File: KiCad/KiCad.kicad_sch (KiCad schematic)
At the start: 20 parts, among them J1 DC-IN, J2 USB4105-GF-A, U1 ESP32-WROOM-32E, U2 MP1584EN, U3 CH340C

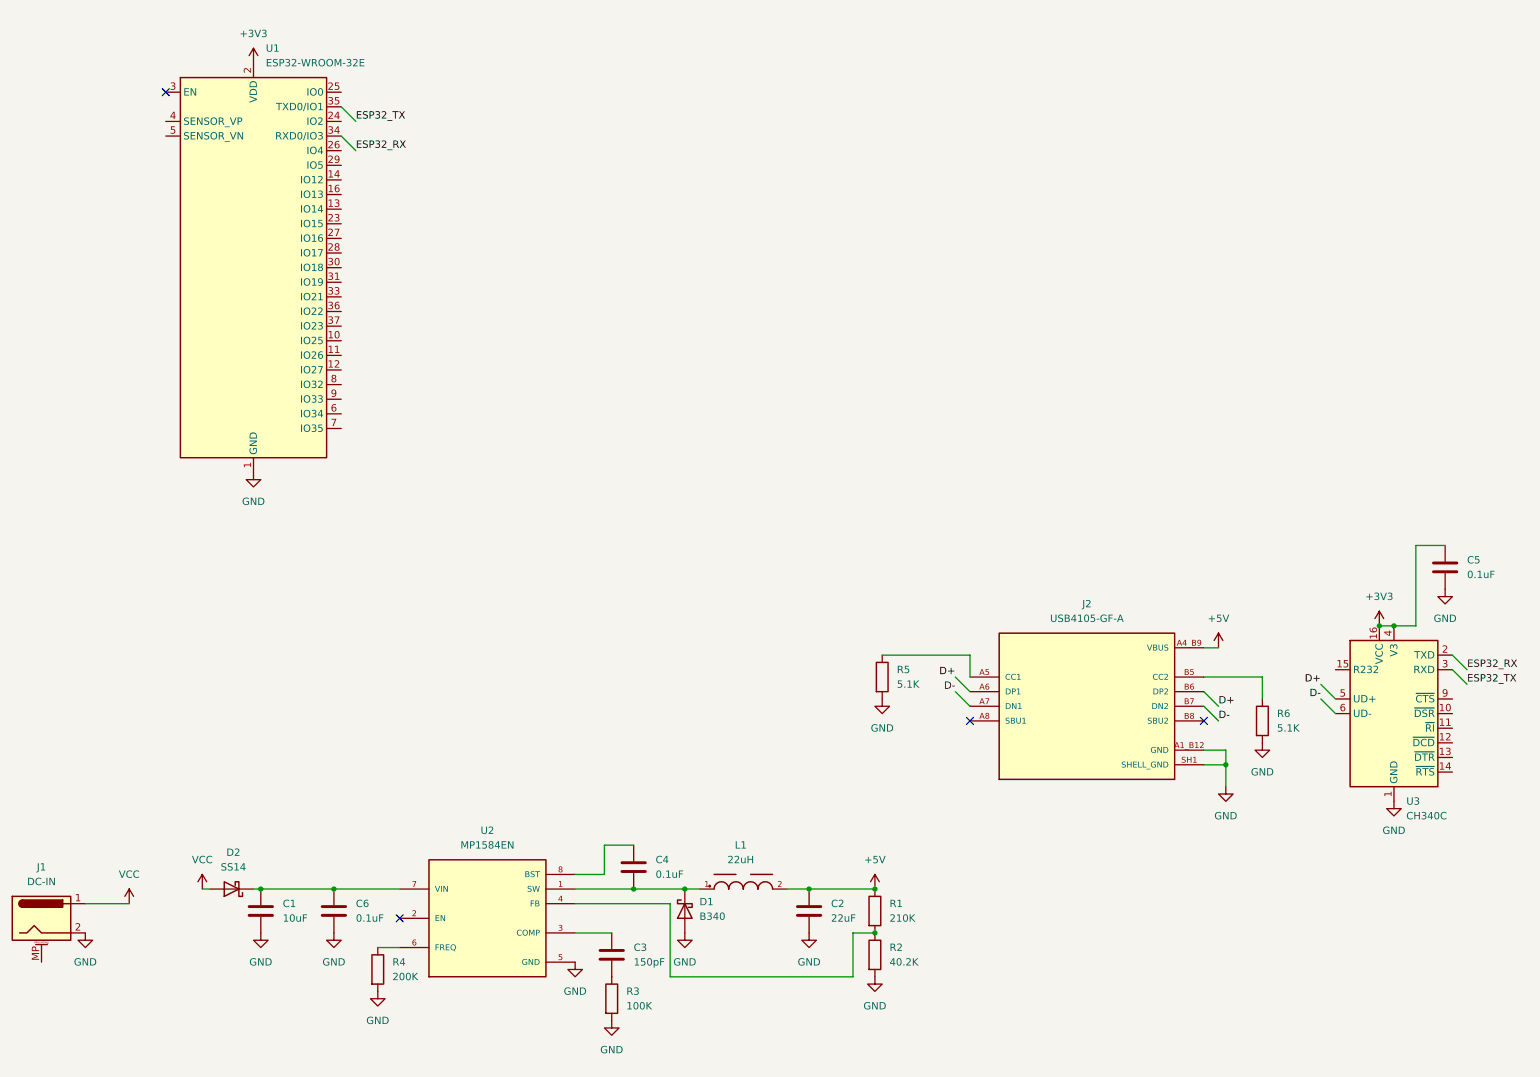
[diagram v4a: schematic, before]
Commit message: 完成5V轉3.3V電源軌元件及防反接電路、ESP32復位電路、優化主電源輸入轉5V的電路、USB轉TTL完整迴路之原理突及PCB
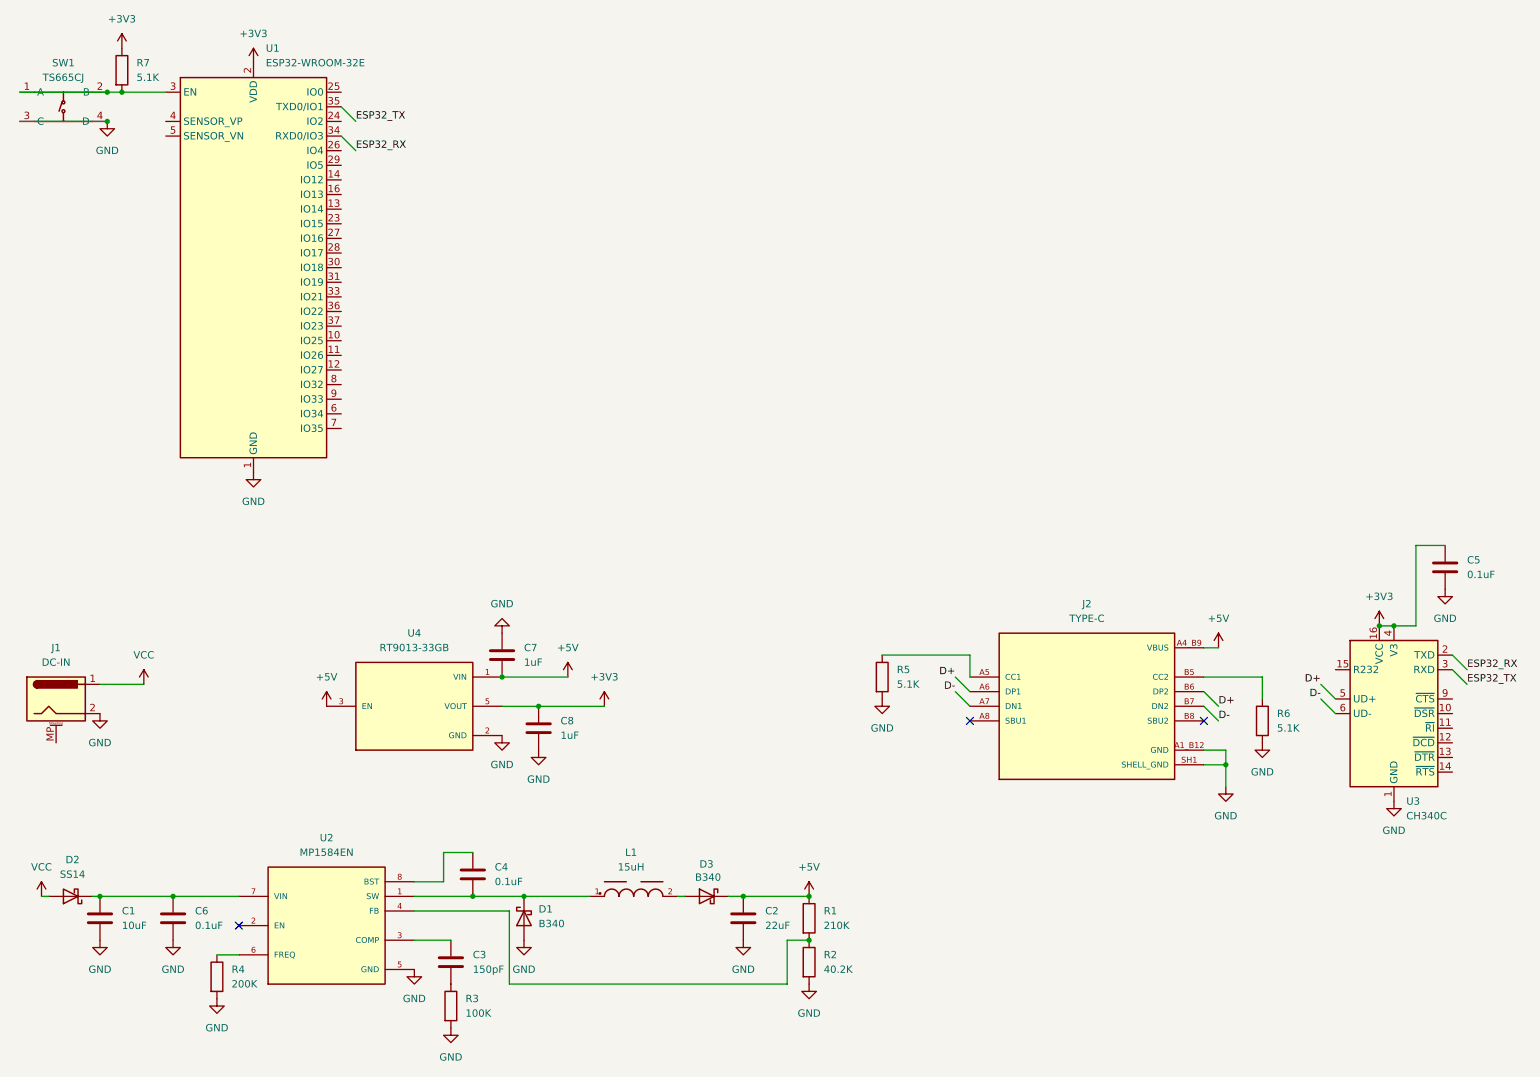
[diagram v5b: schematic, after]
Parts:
- added C7, C8: 1uF, Capacitor_SMD:C_0603_1608Metric, symbol Device:C
- added D3: B340, Diode_SMD:D_SMC, symbol Diode:B340
- added R7: 5.1K, Resistor_SMD:R_0603_1608Metric, symbol Device:R
- added SW1: TS665CJ, button:SW-TH_4P-L6.0-W6.0-P4.50-LS6.5, symbol button:TS665CJ
- added U4: RT9013-33GB, RT9013-33GB:SOT94P279X129-5N, symbol RT9013-33GB:RT9013-33GB
- J2: value USB4105-GF-A -> TYPE-C
- L1: value 22uH -> 15uH
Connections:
- net +3V3: now also C8.1, R7.1, U4.5 (VOUT)
- net +5V: now also C7.2, D3.1 (K), U4.1 (VIN), U4.3 (EN); no longer L1.2
- net GND: now also C7.1, C8.2, SW1.3 (C), SW1.4 (D), U4.2 (GND)
- net at U1.3 (EN): now also R7.2, SW1.1 (A), SW1.2 (B)
- new net: D3.2 (A), L1.2
- no-connect marks 4 -> 3
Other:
- moved on the sheet: C1, C2, C3, C4, C6, D1, D2, J1, L1, R1, R2, R3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

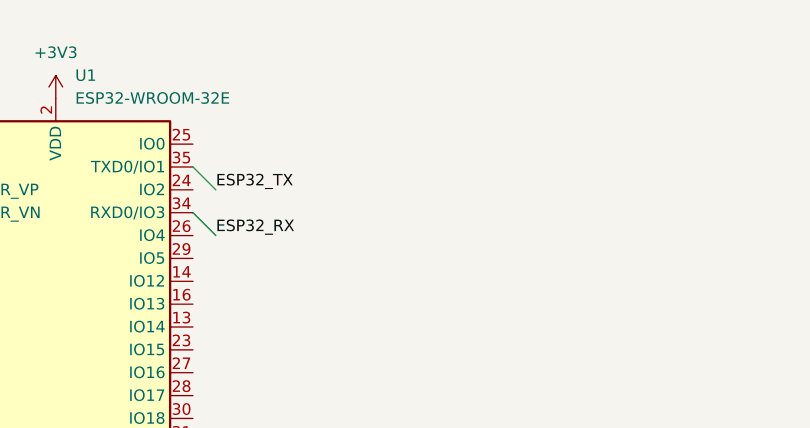
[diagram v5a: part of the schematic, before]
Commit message: 完成esp32的燒錄/工作模式選擇電路之原理圖與PCB
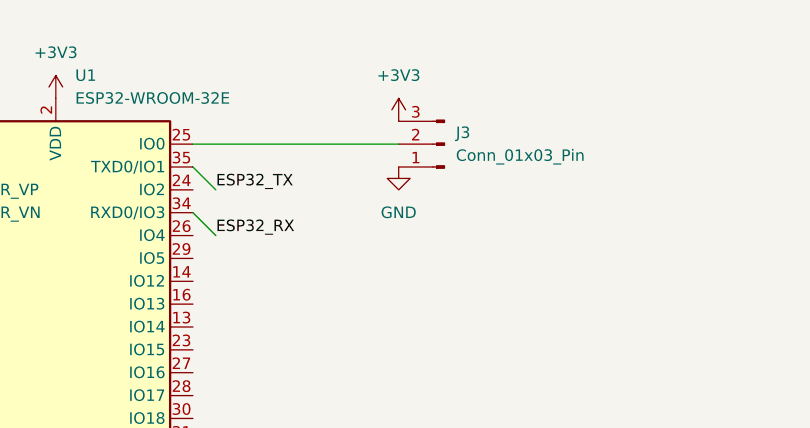
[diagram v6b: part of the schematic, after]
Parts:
- added J3: Conn_01x03_Pin, Connector_PinHeader_2.54mm:PinHeader_1x03_P2.54mm_Vertical, symbol Connector:Conn_01x03_Pin
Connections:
- net +3V3: now also J3.3 (Pin_3)
- net GND: now also J3.1 (Pin_1)
- net at U1.25 (IO0): now also J3.2 (Pin_2)
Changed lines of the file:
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@@
+	(wire
+		(pts
+			(xy 72.39 27.94) (xy 95.25 27.94)
+		)
+		(stroke
+			(width 0)
+			(type default)
+		)
+	)
 	(wire
 		(pts
@@
 	)
 	(symbol
+		(lib_id "Connector:Conn_01x03_Pin")
+		(at 100.33 27.94 180)
+		(unit 1)
+		(exclude_from_sim no)
+		(in_bom yes)
+		(on_board yes)
+		(dnp no)
+		(fields_autoplaced yes)
+		(property "Reference" "J3"
+			(at 101.6 26.6699 0)
+			(effects
+				(font
+					(size 1.27 1.27)
+				)
+				(justify right)
+			)
+		)
+		(property "Value" "Conn_01x03_Pin"
+			(at 101.6 29.2099 0)
+			(effects
+				(font
+					(size 1.27 1.27)
+				)
+				(justify right)
+			)
+		)
+		(property "Footprint" "Connector_PinHeader_2.54mm:PinHeader_1x03_P2.54mm_Vertical"
+			(at 100.33 27.94 0)
+			(effects
+				(font
+					(size 1.27 1.27)
+				)
+				(hide yes)
+			)
+		)
+		(property "Datasheet" "~"
+			(at 100.33 27.94 0)
+			(effects
+				(font
+					(size 1.27 1.27)
+				)
+				(hide yes)
+			)
+		)
+		(property "Description" "Generic connector, single row, 01x03, script generated"
+			(at 100.33 27.94 0)
+			(effects
+				(font
+					(size 1.27 1.27)
+				)
+				(hide yes)
+			)
+		)
+		(pin "1"
+		)
+		(pin "2"
+		)
+		(pin "3"
+		)
+		(instances
+			(project ""
+				(path "/8145d5a2-4aff-47fb-b6a2-0059c8017b6c"
+					(reference "J3")
+					(unit 1)
+				)
+			)
+		)
+	)
+	(symbol
 		(lib_id "Diode:SS14")
 		(at 25.4 167.64 180)
@@
 	)
 	(symbol
+		(lib_id "power:+3V3")
+		(at 95.25 25.4 0)
+		(unit 1)
+		(exclude_from_sim no)
+		(in_bom yes)
+		(on_board yes)
+		(dnp no)
+		(fields_autoplaced yes)
+		(property "Reference" "#PWR031"
+			(at 95.25 29.21 0)
+			(effects
+				(font
+					(size 1.27 1.27)
+				)
+				(hide yes)
+			)
+		)
+		(property "Value" "+3V3"
+			(at 95.25 20.32 0)
+			(effects
+				(font
+					(size 1.27 1.27)
+				)
+			)
+		)
+		(property "Footprint" ""
+			(at 95.25 25.4 0)
+			(effects
+				(font
+					(size 1.27 1.27)
+				)
+				(hide yes)
+			)
+		)
+		(property "Datasheet" ""
+			(at 95.25 25.4 0)
+			(effects
+				(font
+					(size 1.27 1.27)
+				)
+				(hide yes)
+			)
+		)
+		(property "Description" "Power symbol creates a global label with name \"+3V3\""
+			(at 95.25 25.4 0)
+			(effects
+				(font
+					(size 1.27 1.27)
+				)
+				(hide yes)
+			)
+		)
+		(pin "1"
+		)
+		(instances
+			(project "KiCad"
+				(path "/8145d5a2-4aff-47fb-b6a2-0059c8017b6c"
+					(reference "#PWR031")
+					(unit 1)
+				)
+			)
+		)
+	)
+	(symbol
 		(lib_id "Device:R")
 		(at 153.67 171.45 0)
@@
 					(unit 1)
 				)
+			)
+		)
+	)
+	(symbol
+		(lib_id "power:GND")
+		(at 95.25 30.48 0)
+		(unit 1)
+		(exclude_from_sim no)
+		(in_bom yes)
+		(on_board yes)
+		(dnp no)
+		(fields_autoplaced yes)
+		(property "Reference" "#PWR030"
+			(at 95.25 36.83 0)
+			(effects
+				(font
+					(size 1.27 1.27)
+				)
+				(hide yes)
+			)
+		)
+		(property "Value" "GND"
+			(at 95.25 35.56 0)
+			(effects
+				(font
+					(size 1.27 1.27)
+				)
+			)
+		)
+		(property "Footprint" ""
+			(at 95.25 30.48 0)
+			(effects
+				(font
+					(size 1.27 1.27)
+				)
+				(hide yes)
+			)
+		)
+		(property "Datasheet" ""
+			(at 95.25 30.48 0)
+			(effects
+				(font
+					(size 1.27 1.27)
+				)
+				(hide yes)
+			)
+		)
+		(property "Description" "Power symbol creates a global label with name \"GND\" , ground"
+			(at 95.25 30.48 0)
+			(effects
+				(font
+					(size 1.27 1.27)
+				)
+				(hide yes)
+			)
+		)
+		(pin "1"
+		)
+		(instances
+			(project "KiCad"
+				(path "/8145d5a2-4aff-47fb-b6a2-0059c8017b6c"
+					(reference "#PWR030")
+					(unit 1)
+				)

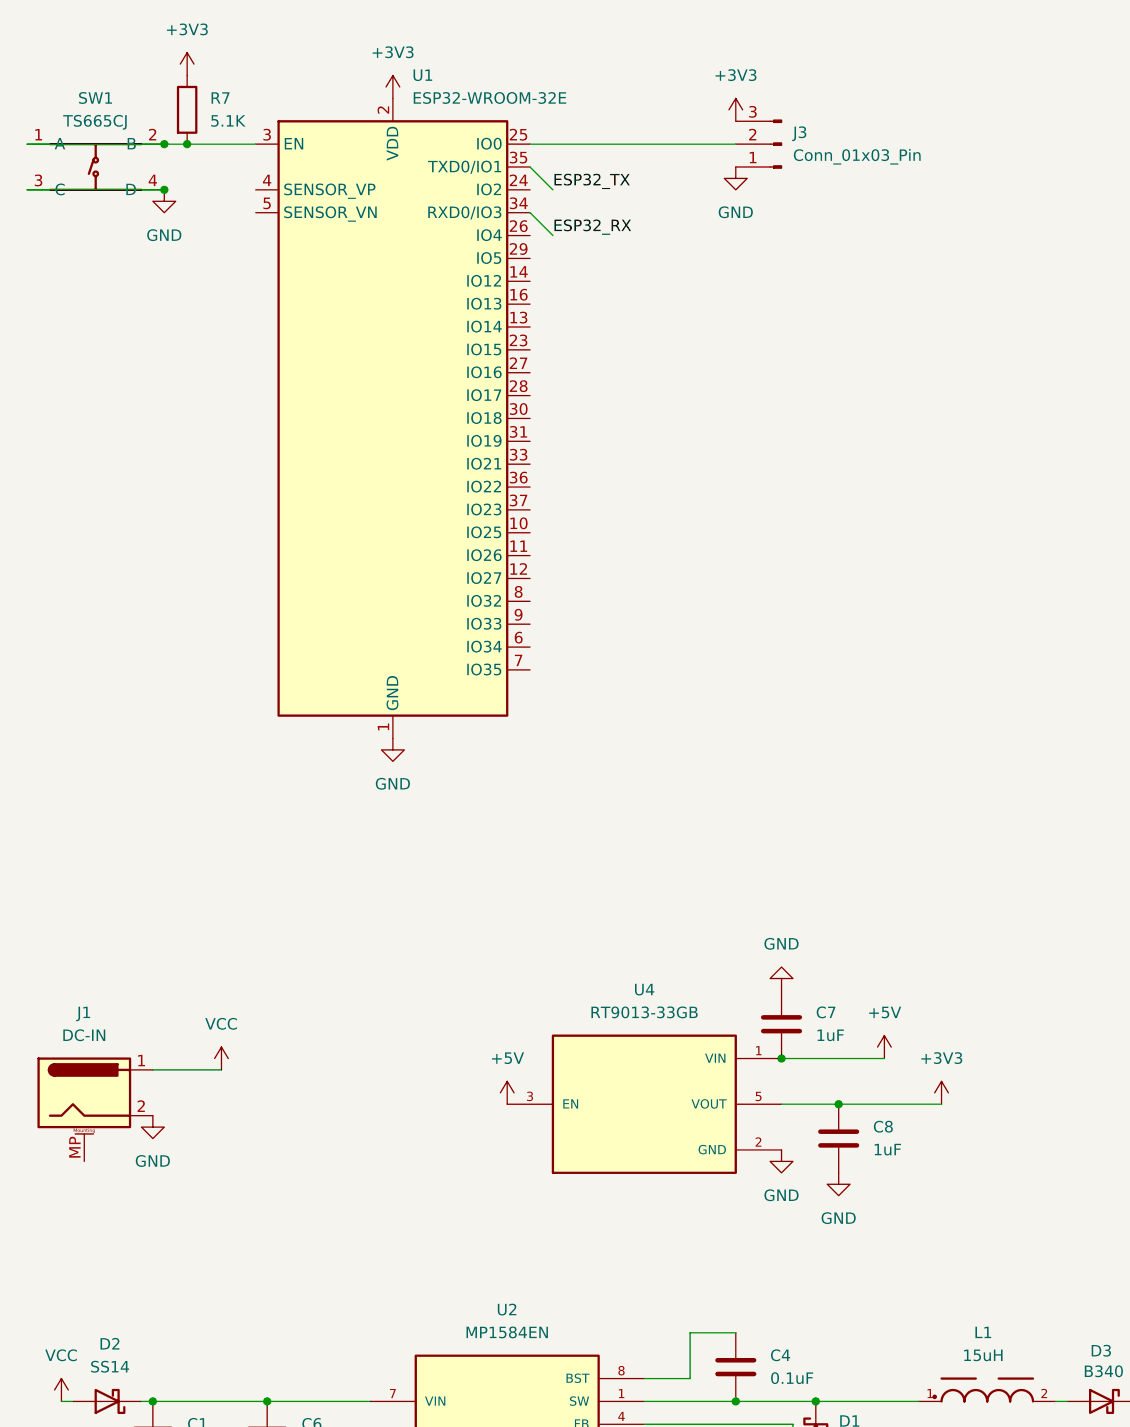
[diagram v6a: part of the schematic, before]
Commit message: 補全mcu供電去偶電容
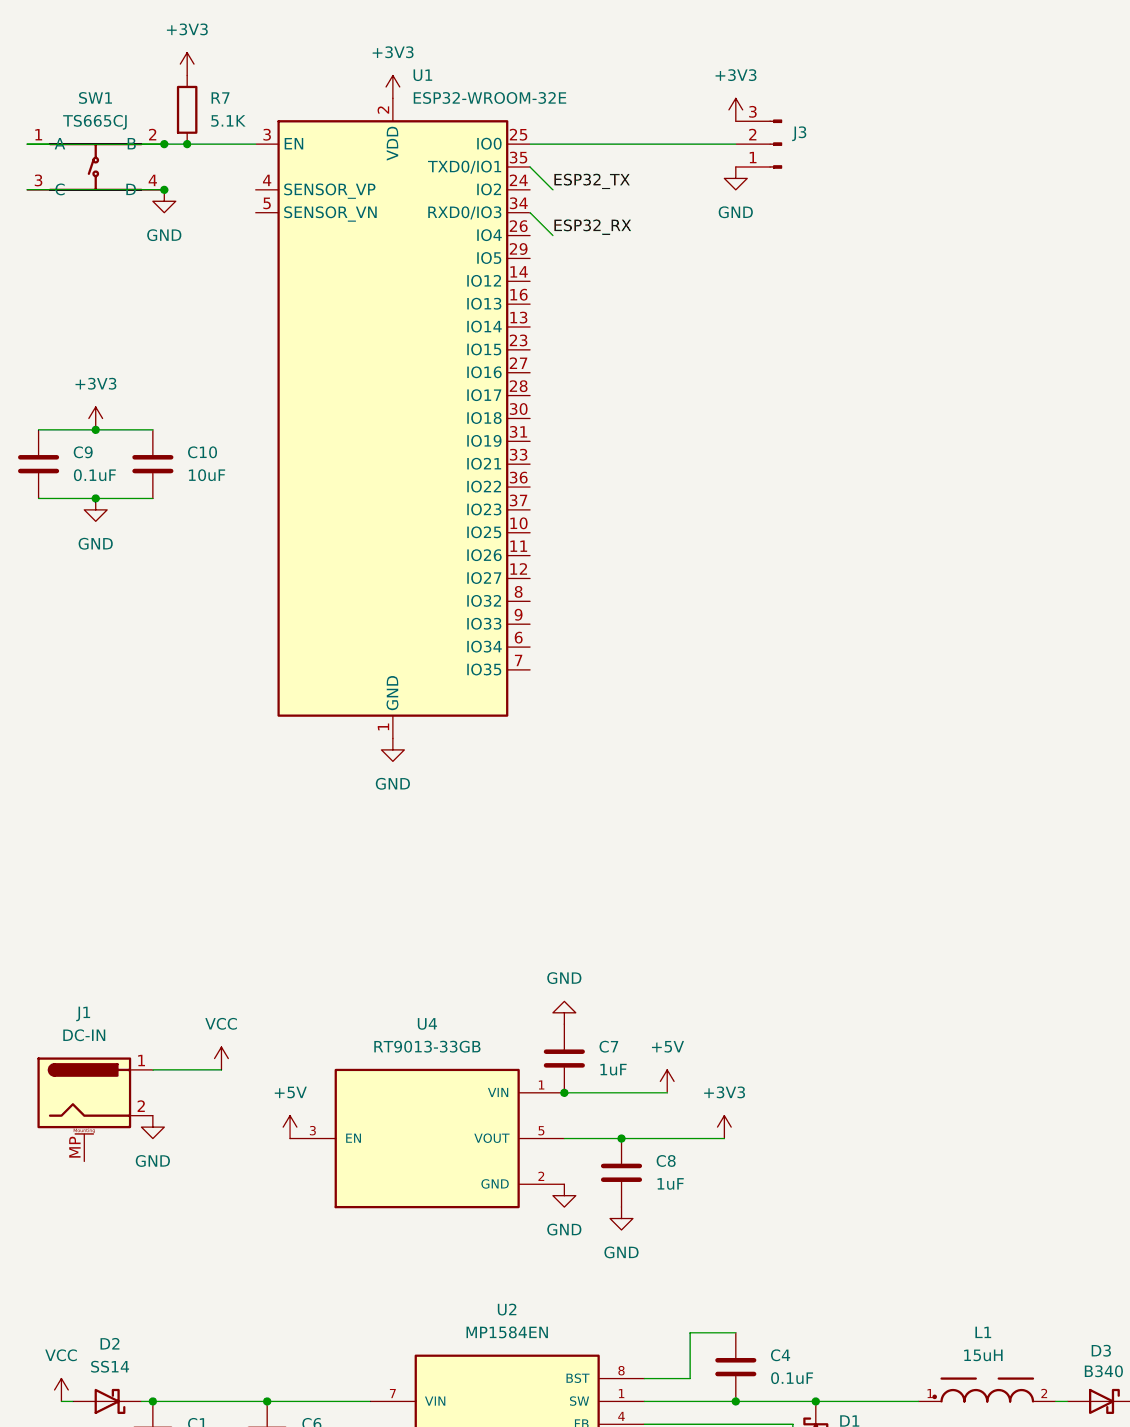
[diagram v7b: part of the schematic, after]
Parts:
- added C10: 10uF, Capacitor_SMD:C_0603_1608Metric, symbol Device:C
- added C9: 0.1uF, Capacitor_SMD:C_0603_1608Metric, symbol Device:C
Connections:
- net +3V3: now also C10.1, C9.1
- net GND: now also C10.2, C9.2
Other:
- moved on the sheet: C7, C8, U4

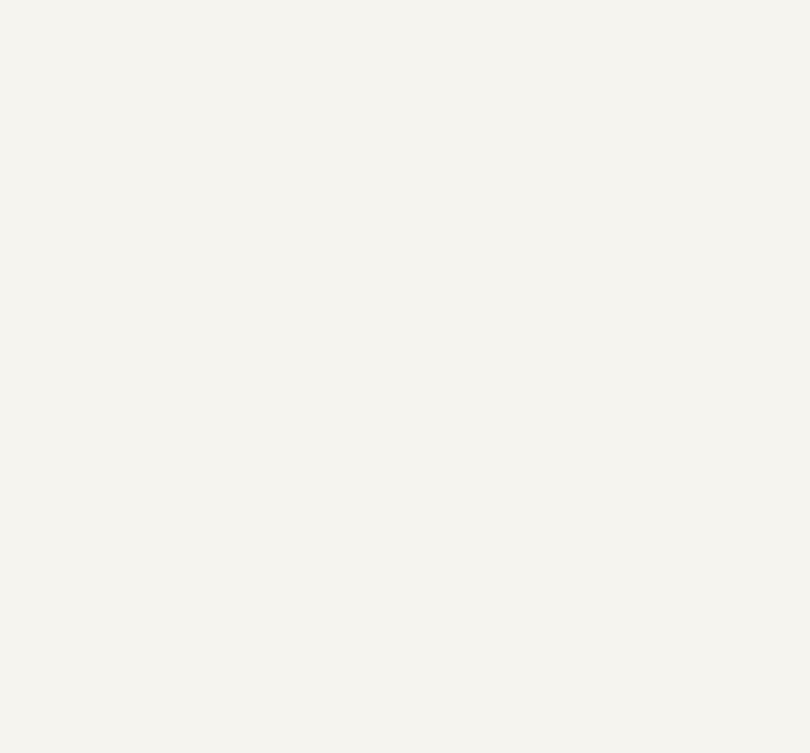
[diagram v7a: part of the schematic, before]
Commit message: 放置0.96吋OLED
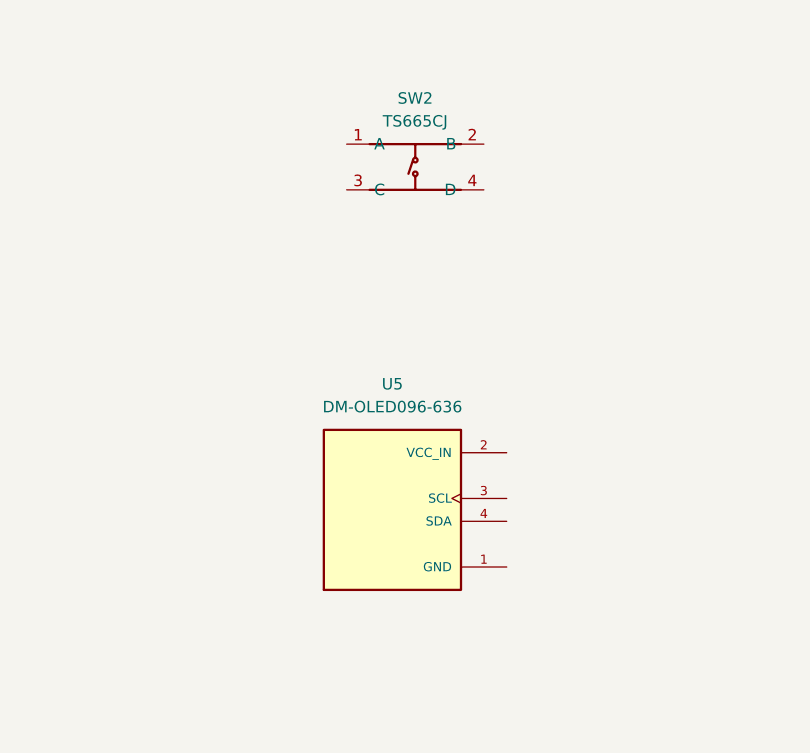
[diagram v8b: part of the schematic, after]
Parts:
- added SW2: TS665CJ, button:SW-TH_4P-L6.0-W6.0-P4.50-LS6.5, symbol button:TS665CJ
- added U5: DM-OLED096-636, OLED:MODULE_DM-OLED096-636, symbol OLED:DM-OLED096-636
